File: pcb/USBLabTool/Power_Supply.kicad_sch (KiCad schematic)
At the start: 54 parts, among them J19 T_N5V, U10 MC33274ADR2G, U11 DG403, U13 R1283K002A, U14 ST1L05APU33R, U15 ST1L05APU33R, U16 LTC1983ES6-5TRMPBF, U9 MC33274ADR2G

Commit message: 1
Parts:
- L5, L6: value 47uH -> 4.7uH
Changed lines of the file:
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@@
 			)
 		)
-		(property "Value" "47uH"
+		(property "Value" "4.7uH"
 			(at 166.624 128.016 90)
 			(effects
@@
 			)
 		)
-		(property "Value" "47uH"
+		(property "Value" "4.7uH"
 			(at 166.116 110.744 90)
 			(effects

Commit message: fixes
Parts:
- C59, C60: value 4.7uF -> 100nF
- L5, L6: footprint Inductor_SMD:L_0603_1608Metric_Pad1.05x0.95mm_HandSolder -> userfp:IND_TAIYO_NRH2410_TAY
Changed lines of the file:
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@@
 			)
 		)
-		(property "Footprint" "Inductor_SMD:L_0603_1608Metric_Pad1.05x0.95mm_HandSolder"
+		(property "Footprint" "userfp:IND_TAIYO_NRH2410_TAY"
 			(at 166.37 130.81 0)
 			(effects
@@
 			)
 		)
+		(property "Purpose" ""
+			(at 166.37 130.81 0)
+			(effects
+				(font
+					(size 1.27 1.27)
+				)
+				(hide yes)
+			)
+		)
 		(pin "1"
 		)
@@
 			)
 		)
-		(property "Value" "4.7uF"
+		(property "Value" "100nF"
 			(at 180.848 119.126 0)
 			(effects
@@
 			)
 		)
-		(property "Value" "4.7uF"
+		(property "Value" "100nF"
 			(at 157.226 118.618 0)
 			(effects
@@
 			)
 		)
-		(property "Footprint" "Inductor_SMD:L_0603_1608Metric_Pad1.05x0.95mm_HandSolder"
+		(property "Footprint" "userfp:IND_TAIYO_NRH2410_TAY"
 			(at 166.37 113.03 0)
 			(effects
@@
 			(at 166.37 113.03 0)
 			(effects
+				(font
+					(size 1.27 1.27)
+				)
+				(hide yes)
+			)
+		)
+		(property "Purpose" ""
+			(at 166.37 113.03 0)
+			(effects

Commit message: PCB V2 updates
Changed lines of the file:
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@@
 	(wire
 		(pts
-			(xy 64.77 133.35) (xy 46.99 133.35)
+			(xy 46.99 133.35) (xy 64.77 133.35)
 		)
 		(stroke

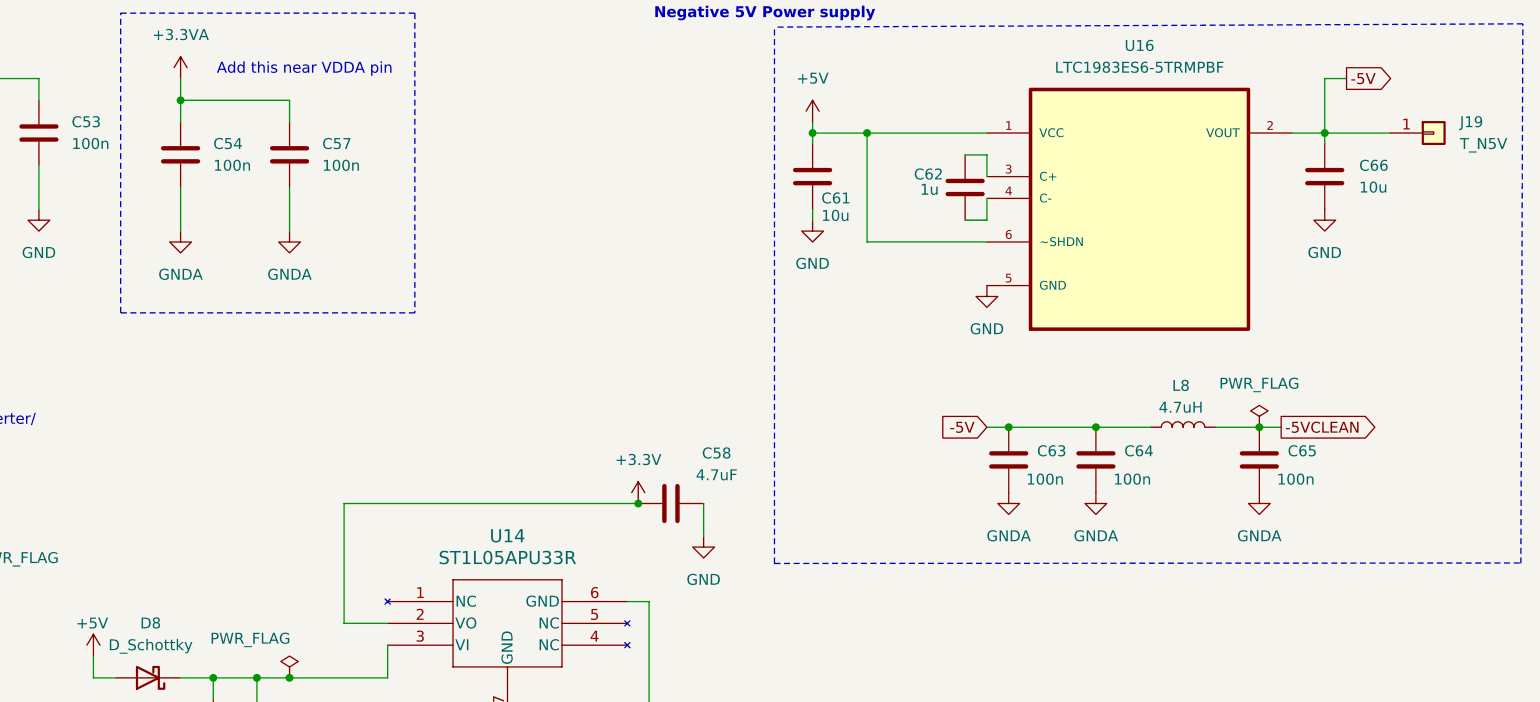
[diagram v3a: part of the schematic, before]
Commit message: update PCB v2 caps
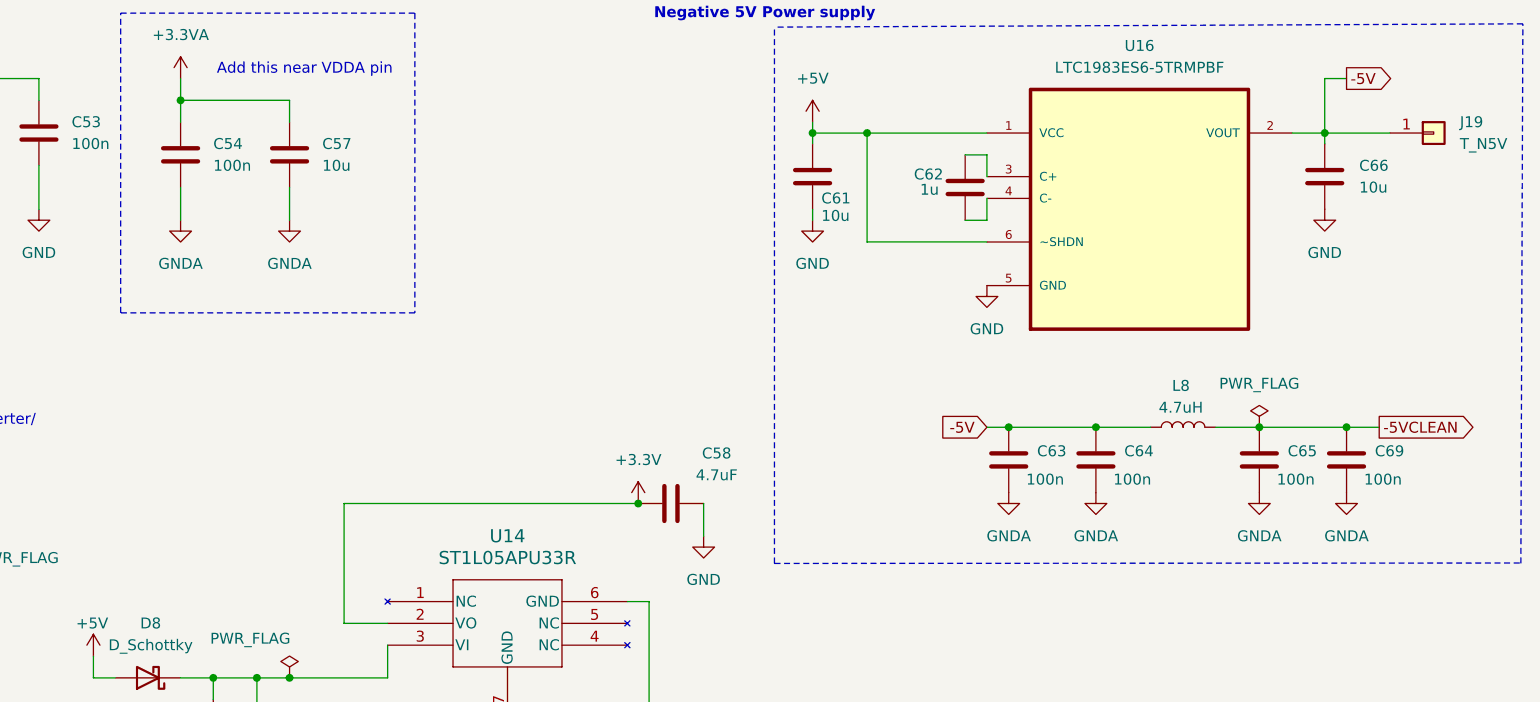
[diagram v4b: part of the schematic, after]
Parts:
- added C69: 100n, Capacitor_SMD:C_0603_1608Metric_Pad1.08x0.95mm_HandSolder, symbol Device:C
- C57: value 100n -> 10u
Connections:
- net -5VCLEAN: now also C69.1
- net GNDA: now also C69.2
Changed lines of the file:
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@@
 	)
 	(junction
+		(at 260.35 67.31)
+		(diameter 0)
+		(color 0 0 0 0)
+	)
+	(junction
 		(at 57.15 26.67)
 		(diameter 0)
@@
 	(wire
 		(pts
-			(xy 137.16 39.37) (xy 137.16 44.45)
+			(xy 137.16 39.37) (xy 137.16 43.18)
 		)
 		(stroke
@@
 	(wire
 		(pts
-			(xy 250.19 67.31) (xy 252.73 67.31)
+			(xy 250.19 67.31) (xy 260.35 67.31)
 		)
 		(stroke
@@
 	(wire
 		(pts
+			(xy 260.35 67.31) (xy 264.16 67.31)
+		)
+		(stroke
+			(width 0)
+			(type default)
+		)
+	)
+	(wire
+		(pts
 			(xy 59.69 82.55) (xy 62.23 82.55)
 		)
@@
 	(wire
 		(pts
-			(xy 124.46 39.37) (xy 124.46 44.45)
+			(xy 124.46 39.37) (xy 124.46 43.18)
 		)
 		(stroke
@@
 	(global_label "-5VCLEAN"
 		(shape output)
-		(at 252.73 67.31 0)
+		(at 264.16 67.31 0)
 		(fields_autoplaced yes)
 		(effects
@@
 		)
 		(property "Intersheetrefs" "${INTERSHEET_REFS}"
-			(at 265.4519 67.31 0)
+			(at 276.8819 67.31 0)
 			(effects
 				(font
@@
 	(symbol
 		(lib_id "power:GNDA")
-		(at 137.16 44.45 0)
+		(at 137.16 43.18 0)
 		(unit 1)
 		(exclude_from_sim no)
@@
 		(fields_autoplaced yes)
 		(property "Reference" "#PWR0111"
-			(at 137.16 50.8 0)
+			(at 137.16 49.53 0)
 			(effects
 				(font
@@
 		)
 		(property "Value" "GNDA"
-			(at 137.16 49.53 0)
+			(at 137.16 48.26 0)
 			(effects
 				(font
@@
 		)
 		(property "Footprint" ""
-			(at 137.16 44.45 0)
+			(at 137.16 43.18 0)
 			(effects
 				(font
@@
 		)
 		(property "Datasheet" ""
-			(at 137.16 44.45 0)
+			(at 137.16 43.18 0)
 			(effects
 				(font
@@
 		)
 		(property "Description" ""
-			(at 137.16 44.45 0)
+			(at 137.16 43.18 0)
 			(effects
 				(font
@@
 	(symbol
 		(lib_id "power:GNDA")
-		(at 124.46 44.45 0)
+		(at 124.46 43.18 0)
 		(unit 1)
 		(exclude_from_sim no)
@@
 		(fields_autoplaced yes)
 		(property "Reference" "#PWR0108"
-			(at 124.46 50.8 0)
+			(at 124.46 49.53 0)
 			(effects
 				(font
@@
 		)
 		(property "Value" "GNDA"
-			(at 124.46 49.53 0)
+			(at 124.46 48.26 0)
 			(effects
 				(font
@@
 		)
 		(property "Footprint" ""
-			(at 124.46 44.45 0)
+			(at 124.46 43.18 0)
 			(effects
 				(font
@@
 		)
 		(property "Datasheet" ""
-			(at 124.46 44.45 0)
+			(at 124.46 43.18 0)
 			(effects
 				(font
@@
 		)
 		(property "Description" ""
-			(at 124.46 44.45 0)
+			(at 124.46 43.18 0)
 			(effects
 				(font
@@
 	(symbol
 		(lib_id "power:GNDA")
+		(at 260.35 74.93 0)
+		(unit 1)
+		(exclude_from_sim no)
+		(in_bom yes)
+		(on_board yes)
+		(dnp no)
+		(fields_autoplaced yes)
+		(property "Reference" "#PWR0127"
+			(at 260.35 81.28 0)
+			(effects
+				(font
+					(size 1.27 1.27)
+				)
+				(hide yes)
+			)
+		)
+		(property "Value" "GNDA"
+			(at 260.35 80.01 0)
+			(effects
+				(font
+					(size 1.27 1.27)
+				)
+			)
+		)
+		(property "Footprint" ""
+			(at 260.35 74.93 0)
+			(effects
+				(font
+					(size 1.27 1.27)
+				)
+				(hide yes)
+			)
+		)
+		(property "Datasheet" ""
+			(at 260.35 74.93 0)
+			(effects
+				(font
+					(size 1.27 1.27)
+				)
+				(hide yes)
+			)
+		)
+		(property "Description" "Power symbol creates a global label with name \"GNDA\" , analog ground"
+			(at 260.35 74.93 0)
+			(effects
+				(font
+					(size 1.27 1.27)
+				)
+				(hide yes)
+			)
+		)
+		(pin "1"
+		)
+		(instances
+			(project "USBLabTool"
+				(path "/b5440f7d-90d5-417e-adc2-aa6b11e5424d/eb849fef-899c-46da-8ce0-ed0caaa370cf"
+					(reference "#PWR0127")
+					(unit 1)
+				)
+			)
+		)
+	)
+	(symbol
+		(lib_id "power:GNDA")
 		(at 167.64 163.83 0)
 		(unit 1)
@@
 			)
 		)
-		(property "Value" "100n"
+		(property "Value" "10u"
 			(at 140.97 36.8299 0)
 			(effects
@@
 					(unit 1)
 				)
+			)
+		)
+	)
+	(symbol
+		(lib_id "Device:C")
+		(at 260.35 71.12 0)
+		(unit 1)
+		(exclude_from_sim no)
+		(in_bom yes)
+		(on_board yes)
+		(dnp no)
+		(property "Reference" "C69"
+			(at 263.652 70.104 0)
+			(effects
+				(font
+					(size 1.27 1.27)
+				)
+				(justify left)
+			)
+		)
+		(property "Value" "100n"
+			(at 262.382 73.406 0)
+			(effects
+				(font
+					(size 1.27 1.27)
+				)
+				(justify left)
+			)
+		)
+		(property "Footprint" "Capacitor_SMD:C_0603_1608Metric_Pad1.08x0.95mm_HandSolder"
+			(at 261.3152 74.93 0)
+			(effects
+				(font
+					(size 1.27 1.27)
+				)
+				(hide yes)
+			)
+		)
+		(property "Datasheet" "~"
+			(at 260.35 71.12 0)
+			(effects
+				(font
+					(size 1.27 1.27)
+				)
+				(hide yes)
+			)
+		)
+		(property "Description" ""
+			(at 260.35 71.12 0)
+			(effects
+				(font
+					(size 1.27 1.27)
+				)
+				(hide yes)
+			)
+		)
+		(pin "1"
+		)
+		(pin "2"
+		)
+		(instances
+			(project "USBLabTool"
+				(path "/b5440f7d-90d5-417e-adc2-aa6b11e5424d/eb849fef-899c-46da-8ce0-ed0caaa370cf"
+					(reference "C69")
+					(unit 1)
+				)

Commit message: update pcb v2
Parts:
- removed C69: 100n, Capacitor_SMD:C_0603_1608Metric_Pad1.08x0.95mm_HandSolder, symbol Device:C
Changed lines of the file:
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@@
 	)
 	(junction
-		(at 260.35 67.31)
-		(diameter 0)
-		(color 0 0 0 0)
-	)
-	(junction
 		(at 57.15 26.67)
 		(diameter 0)
@@
 	(wire
 		(pts
-			(xy 250.19 67.31) (xy 260.35 67.31)
-		)
-		(stroke
-			(width 0)
-			(type default)
-		)
-	)
-	(wire
-		(pts
 			(xy 133.35 96.52) (xy 133.35 153.67)
 		)
@@
 	(wire
 		(pts
-			(xy 260.35 67.31) (xy 264.16 67.31)
+			(xy 250.19 67.31) (xy 264.16 67.31)
 		)
 		(stroke
@@
 	(symbol
 		(lib_id "power:GNDA")
-		(at 260.35 74.93 0)
-		(unit 1)
-		(exclude_from_sim no)
-		(in_bom yes)
-		(on_board yes)
-		(dnp no)
-		(fields_autoplaced yes)
-		(property "Reference" "#PWR0127"
-			(at 260.35 81.28 0)
-			(effects
-				(font
-					(size 1.27 1.27)
-				)
-				(hide yes)
-			)
-		)
-		(property "Value" "GNDA"
-			(at 260.35 80.01 0)
-			(effects
-				(font
-					(size 1.27 1.27)
-				)
-			)
-		)
-		(property "Footprint" ""
-			(at 260.35 74.93 0)
-			(effects
-				(font
-					(size 1.27 1.27)
-				)
-				(hide yes)
-			)
-		)
-		(property "Datasheet" ""
-			(at 260.35 74.93 0)
-			(effects
-				(font
-					(size 1.27 1.27)
-				)
-				(hide yes)
-			)
-		)
-		(property "Description" "Power symbol creates a global label with name \"GNDA\" , analog ground"
-			(at 260.35 74.93 0)
-			(effects
-				(font
-					(size 1.27 1.27)
-				)
-				(hide yes)
-			)
-		)
-		(pin "1"
-		)
-		(instances
-			(project "USBLabTool"
-				(path "/b5440f7d-90d5-417e-adc2-aa6b11e5424d/eb849fef-899c-46da-8ce0-ed0caaa370cf"
-					(reference "#PWR0127")
-					(unit 1)
-				)
-			)
-		)
-	)
-	(symbol
-		(lib_id "power:GNDA")
 		(at 167.64 163.83 0)
 		(unit 1)
@@
 					(unit 1)
 				)
-			)
-		)
-	)
-	(symbol
-		(lib_id "Device:C")
-		(at 260.35 71.12 0)
-		(unit 1)
-		(exclude_from_sim no)
-		(in_bom yes)
-		(on_board yes)
-		(dnp no)
-		(property "Reference" "C69"
-			(at 263.652 70.104 0)
-			(effects
-				(font
-					(size 1.27 1.27)
-				)
-				(justify left)
-			)
-		)
-		(property "Value" "100n"
-			(at 262.382 73.406 0)
-			(effects
-				(font
-					(size 1.27 1.27)
-				)
-				(justify left)
-			)
-		)
-		(property "Footprint" "Capacitor_SMD:C_0603_1608Metric_Pad1.08x0.95mm_HandSolder"
-			(at 261.3152 74.93 0)
-			(effects
-				(font
-					(size 1.27 1.27)
-				)
-				(hide yes)
-			)
-		)
-		(property "Datasheet" "~"
-			(at 260.35 71.12 0)
-			(effects
-				(font
-					(size 1.27 1.27)
-				)
-				(hide yes)
-			)
-		)
-		(property "Description" ""
-			(at 260.35 71.12 0)
-			(effects
-				(font
-					(size 1.27 1.27)
-				)
-				(hide yes)
-			)
-		)
-		(pin "1"
-		)
-		(pin "2"
-		)
-		(instances
-			(project "USBLabTool"
-				(path "/b5440f7d-90d5-417e-adc2-aa6b11e5424d/eb849fef-899c-46da-8ce0-ed0caaa370cf"
-					(reference "C69")
-					(unit 1)
-				)
